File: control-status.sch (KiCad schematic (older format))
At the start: 11 parts

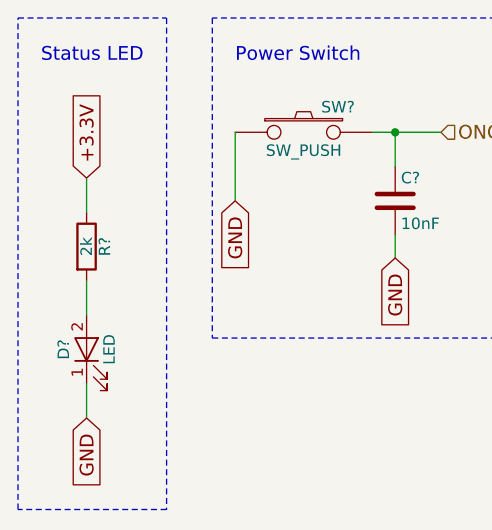
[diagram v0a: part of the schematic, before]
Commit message: this version contains the datasheets and the footprints of the parts
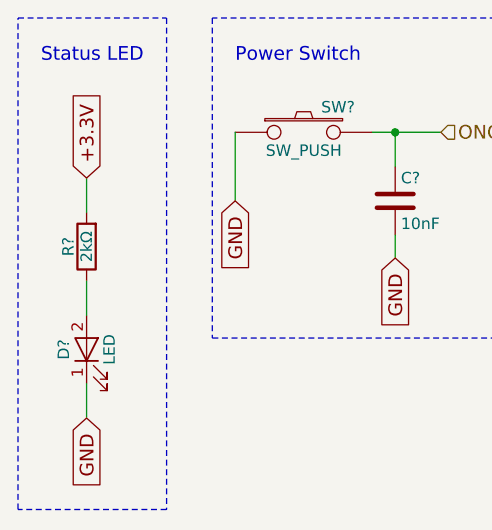
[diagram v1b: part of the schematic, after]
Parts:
- removed C? (x2): 100nF, symbol C
- removed R?: 2k, symbol R
- removed SW?: SW_PUSH, symbol SW_PUSH
- added C? (x2): 100nF, Capacitors_SMD:C_0603_HandSoldering, symbol C
- added R?: 2kΩ, Resistors_SMD:R_0603_HandSoldering, symbol R
- added SW?: SW_PUSH, water:EVQQ2202W, symbol SW_PUSH
- C?: footprint (none) -> Capacitors_SMD:C_0603_HandSoldering
- SW?: footprint (none) -> water:EVQQ2202W; alt (none) -> http://hu.farnell.com/alcoswitch-te-connectivity/fsm2jrt/ta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
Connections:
- net +3.3V: now also C?.1, R?.2
- net GND: now also C?.2, C?.2, SW?.2
- net RESET: now also C?.1, SW?.1
- net at D?.2 (A): now also R?.1
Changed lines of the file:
@@
 Comment4 ""
 $EndDescr
-$Comp
-L R R?
-U 1 1 59A3B272
-P 1050 1750
-F 0 "R?" V 1130 1750 50  0000 C CNN
-F 1 "2k" V 1050 1750 50  0000 C CNN
-F 2 "" V 980 1750 50  0001 C CNN
-F 3 "" H 1050 1750 50  0001 C CNN
-	1    1050 1750
-	1    0    0    -1
-$EndComp
 Text GLabel 1050 1450 1    60   Input ~ 0
 +3.3V
@@
 F 0 "SW?" H 2150 1360 50  0000 C CNN
 F 1 "SW_PUSH" H 2000 1170 50  0000 C CNN
-F 2 "" H 2000 1250 60  0000 C CNN
-F 3 "" H 2000 1250 60  0000 C CNN
+F 2 "water:EVQQ2202W" H 2000 1250 60  0001 C CNN
+F 3 "http://hu.farnell.com/panasonic-electronic-components/evqq2202w/switch-smd-6-5x6x2-5mm-3-5n/dp/1821261" H 2000 1250 60  0001 C CNN
+F 4 "http://hu.farnell.com/alcoswitch-te-connectivity/fsm2jrt/tactile-switch-spst-no-0-05a-24v/dp/2610957" H 2000 1250 60  0001 C CNN "alt"
 	1    2000 1250
 	1    0    0    -1
@@
 F 0 "C?" H 2425 1650 50  0000 L CNN
 F 1 "10nF" H 2425 1450 50  0000 L CNN
-F 2 "" H 2438 1400 50  0001 C CNN
-F 3 "" H 2400 1550 50  0001 C CNN
+F 2 "Capacitors_SMD:C_0603_HandSoldering" H 2438 1400 50  0001 C CNN
+F 3 "http://hu.farnell.com/multicomp/mc0603b103k500ct/cap-mlcc-x7r-10nf-50v-0603/dp/1759102" H 2400 1550 50  0001 C CNN
 	1    2400 1550
 	1    0    0    -1
@@
 Text Notes 4150 900  0    60   ~ 0
 Reset
-$Comp
-L SW_PUSH SW?
-U 1 1 59A3D04B
-P 5200 1350
-F 0 "SW?" H 5350 1460 50  0000 C CNN
-F 1 "SW_PUSH" H 5200 1270 50  0000 C CNN
-F 2 "" H 5200 1350 60  0000 C CNN
-F 3 "" H 5200 1350 60  0000 C CNN
-	1    5200 1350
-	1    0    0    -1
-$EndComp
 Text GLabel 5650 1700 3    60   Input ~ 0
 GND
-$Comp
-L C C?
-U 1 1 59A3D4AC
-P 4900 1550
-F 0 "C?" H 4925 1650 50  0000 L CNN
-F 1 "100nF" H 4925 1450 50  0000 L CNN
-F 2 "" H 4938 1400 50  0001 C CNN
-F 3 "" H 4900 1550 50  0001 C CNN
-	1    4900 1550
-	1    0    0    -1
-$EndComp
 Text GLabel 4900 1700 3    60   Input ~ 0
 GND
 Text HLabel 4900 1300 1    60   Input ~ 0
 RESET
-$Comp
-L C C?
-U 1 1 59A3E1D3
-P 4150 1650
-F 0 "C?" H 4175 1750 50  0000 L CNN
-F 1 "100nF" H 4175 1550 50  0000 L CNN
-F 2 "" H 4188 1500 50  0001 C CNN
-F 3 "" H 4150 1650 50  0001 C CNN
-	1    4150 1650
-	1    0    0    -1
-$EndComp
 Text GLabel 4150 1950 3    60   Input ~ 0
 GND
@@
 Wire Notes Line
 	6400 3500 1200 3500
+$Comp
+L C C?
+U 1 1 59A6A0B2
+P 4900 1550
+F 0 "C?" H 4925 1650 50  0000 L CNN
+F 1 "100nF" H 4925 1450 50  0000 L CNN
+F 2 "Capacitors_SMD:C_0603_HandSoldering" H 4938 1400 30  0001 C CNN
+F 3 "hu.farnell.com/avx/06035c104kat2a/cap-mlcc-x7r-100nf-50v-0603/dp/1301804" H 4900 1550 60  0001 C CNN
+	1    4900 1550
+	1    0    0    -1
+$EndComp
+$Comp
+L C C?
+U 1 1 59A6A9F5
+P 4150 1650
+F 0 "C?" H 4175 1750 50  0000 L CNN
+F 1 "100nF" H 4175 1550 50  0000 L CNN
+F 2 "Capacitors_SMD:C_0603_HandSoldering" H 4188 1500 30  0001 C CNN
+F 3 "hu.farnell.com/avx/06035c104kat2a/cap-mlcc-x7r-100nf-50v-0603/dp/1301804" H 4150 1650 60  0001 C CNN
+	1    4150 1650
+	1    0    0    -1
+$EndComp
+$Comp
+L SW_PUSH SW?
+U 1 1 59A6C82D
+P 5200 1350
+F 0 "SW?" H 5350 1460 50  0000 C CNN
+F 1 "SW_PUSH" H 5200 1270 50  0000 C CNN
+F 2 "water:EVQQ2202W" H 5200 1350 60  0001 C CNN
+F 3 "http://hu.farnell.com/panasonic-electronic-components/evqq2202w/switch-smd-6-5x6x2-5mm-3-5n/dp/1821261" H 5200 1350 60  0001 C CNN
+F 4 "http://hu.farnell.com/alcoswitch-te-connectivity/fsm2jrt/tactile-switch-spst-no-0-05a-24v/dp/2610957" H 5200 1350 60  0001 C CNN "alt"
+	1    5200 1350
+	1    0    0    -1
+$EndComp
+$Comp
+L R R?
+U 1 1 59A95521
+P 1050 1750
+F 0 "R?" V 1130 1750 50  0000 C CNN
+F 1 "2kΩ" V 1050 1750 50  0000 C CNN
+F 2 "Resistors_SMD:R_0603_HandSoldering" V 980 1750 50  0001 C CNN
+F 3 "hu.farnell.com/multicomp/mcwr06x2001ftl/res-thick-film-2k-1-0-1w-0603/dp/2447319" H 1050 1750 50  0001 C CNN
+	1    1050 1750
+	-1   0    0    1
+$EndComp
 $EndSCHEMATC

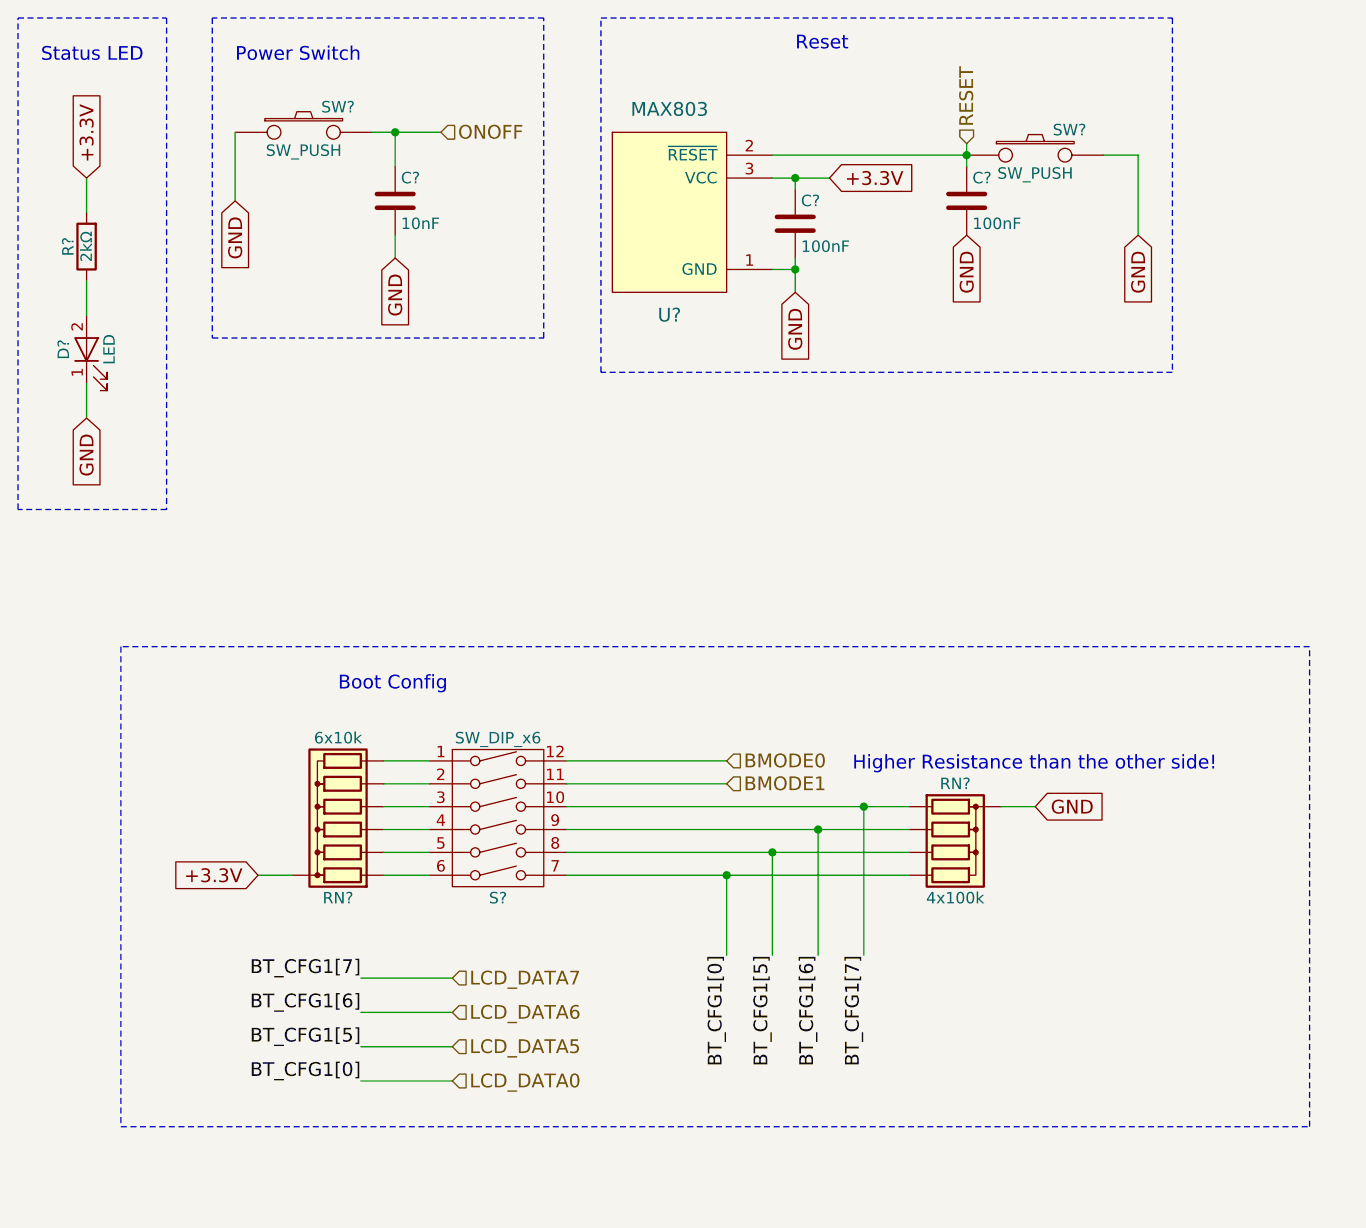
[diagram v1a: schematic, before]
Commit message: some issues fixed by the bugfixer; formal verification needed
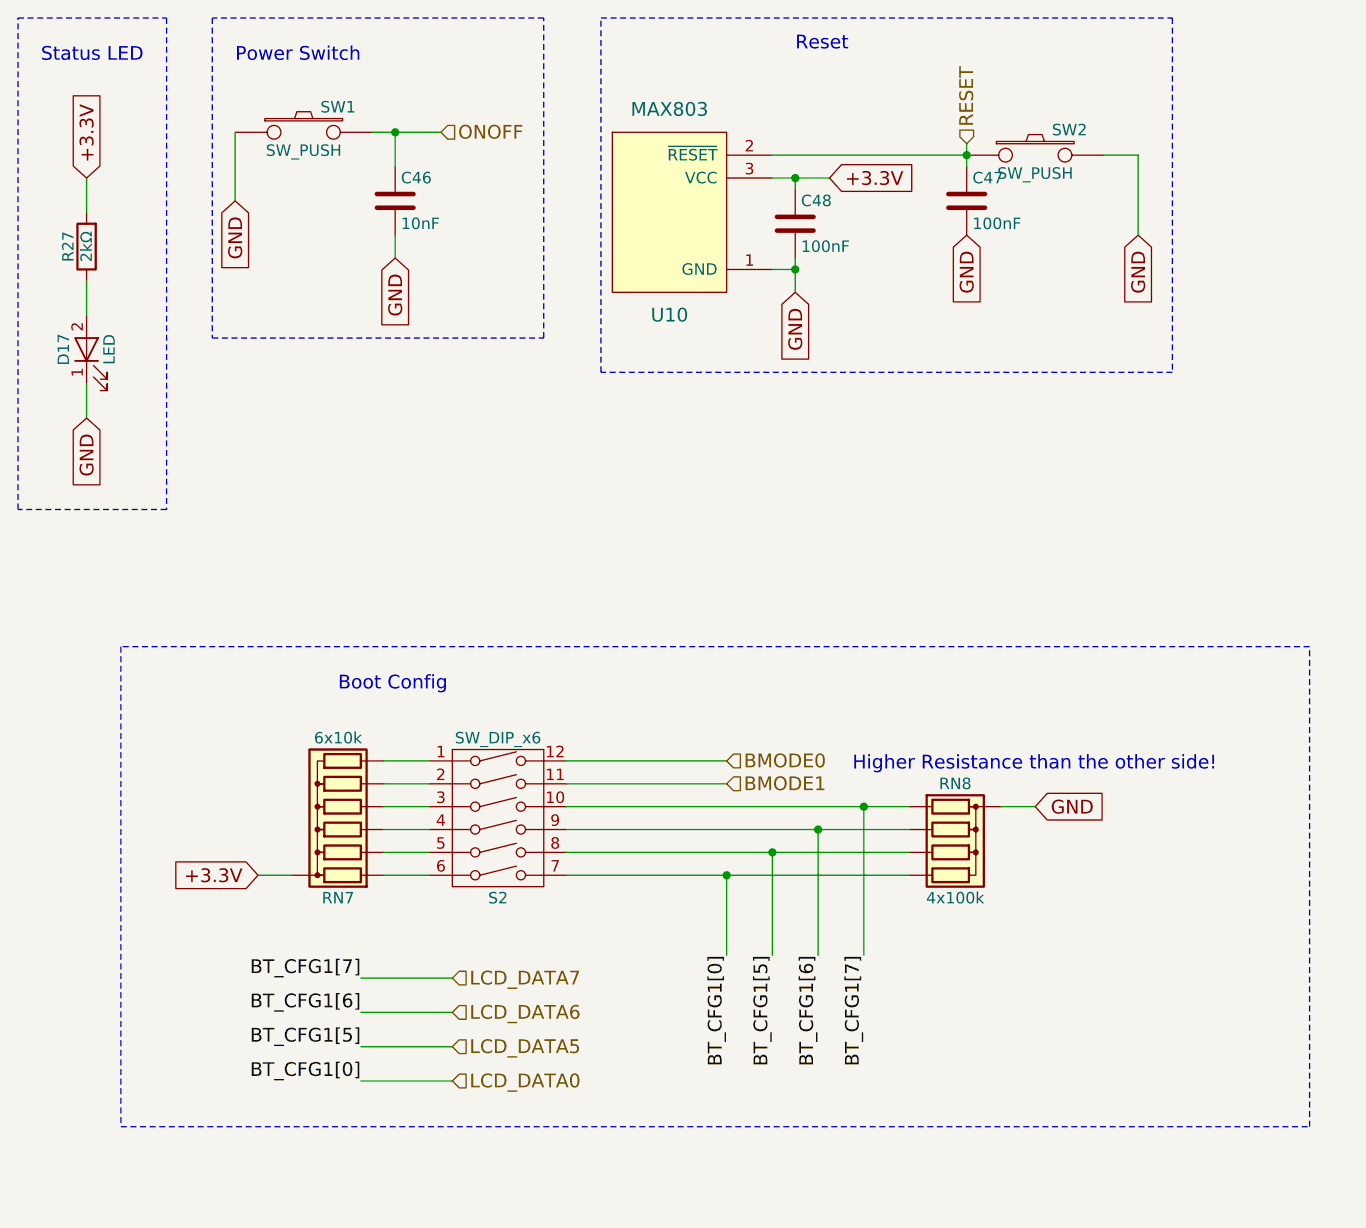
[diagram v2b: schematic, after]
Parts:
- gave numbers to parts that had none: 11
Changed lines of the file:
@@
 Status LED
 $Comp
-L LED D?
+L LED D17
 U 1 1 59A3B634
 P 1050 2200
-F 0 "D?" H 1050 2300 50  0000 C CNN
+F 0 "D17" H 1050 2300 50  0000 C CNN
 F 1 "LED" H 1050 2100 50  0000 C CNN
 F 2 "" H 1050 2200 50  0001 C CNN
@@
 Power Switch
 $Comp
-L SW_PUSH SW?
+L SW_PUSH SW1
 U 1 1 59A3BABB
 P 2000 1250
-F 0 "SW?" H 2150 1360 50  0000 C CNN
+F 0 "SW1" H 2150 1360 50  0000 C CNN
 F 1 "SW_PUSH" H 2000 1170 50  0000 C CNN
 F 2 "water:EVQQ2202W" H 2000 1250 60  0001 C CNN
@@
 GND
 $Comp
-L C C?
+L C C46
 U 1 1 59A3BB74
 P 2400 1550
-F 0 "C?" H 2425 1650 50  0000 L CNN
+F 0 "C46" H 2425 1650 50  0000 L CNN
 F 1 "10nF" H 2425 1450 50  0000 L CNN
 F 2 "Capacitors_SMD:C_0603_HandSoldering" H 2438 1400 50  0001 C CNN
@@
 GND
 $Comp
-L MAX803 U?
+L MAX803 U10
 U 1 1 59A3F36D
 P 3900 1200
-F 0 "U?" H 3600 350 60  0000 C CNN
+F 0 "U10" H 3600 350 60  0000 C CNN
 F 1 "MAX803" H 3600 1250 60  0000 C CNN
 F 2 "" H 3900 1200 60  0001 C CNN
@@
 +3.3V
 $Comp
-L SW_DIP_x6 S?
+L SW_DIP_x6 S2
 U 1 1 59A40F18
 P 2850 4250
-F 0 "S?" H 2850 3900 50  0000 C CNN
+F 0 "S2" H 2850 3900 50  0000 C CNN
 F 1 "SW_DIP_x6" H 2850 4600 50  0000 C CNN
 F 2 "" H 2800 4250 60  0000 C CNN
@@
 $EndComp
 $Comp
-L R_Network06 RN?
+L R_Network06 RN7
 U 1 1 59A4135A
 P 2150 4200
-F 0 "RN?" V 1750 4200 50  0000 C CNN
+F 0 "RN7" V 1750 4200 50  0000 C CNN
 F 1 "6x10k" V 2450 4200 50  0000 C CNN
 F 2 "Resistors_THT:R_Array_SIP7" V 2525 4200 50  0001 C CNN
@@
 BMODE1
 $Comp
-L R_Network04 RN?
+L R_Network04 RN8
 U 1 1 59A43007
 P 4850 4400
-F 0 "RN?" V 4550 4400 50  0000 C CNN
+F 0 "RN8" V 4550 4400 50  0000 C CNN
 F 1 "4x100k" V 5050 4400 50  0000 C CNN
 F 2 "Resistors_THT:R_Array_SIP5" V 5125 4400 50  0001 C CNN
@@
 	6400 3500 1200 3500
 $Comp
-L C C?
+L C C47
 U 1 1 59A6A0B2
 P 4900 1550
-F 0 "C?" H 4925 1650 50  0000 L CNN
+F 0 "C47" H 4925 1650 50  0000 L CNN
 F 1 "100nF" H 4925 1450 50  0000 L CNN
 F 2 "Capacitors_SMD:C_0603_HandSoldering" H 4938 1400 30  0001 C CNN
@@
 $EndComp
 $Comp
-L C C?
+L C C48
 U 1 1 59A6A9F5
 P 4150 1650
-F 0 "C?" H 4175 1750 50  0000 L CNN
+F 0 "C48" H 4175 1750 50  0000 L CNN
 F 1 "100nF" H 4175 1550 50  0000 L CNN
 F 2 "Capacitors_SMD:C_0603_HandSoldering" H 4188 1500 30  0001 C CNN
@@
 $EndComp
 $Comp
-L SW_PUSH SW?
+L SW_PUSH SW2
 U 1 1 59A6C82D
 P 5200 1350
-F 0 "SW?" H 5350 1460 50  0000 C CNN
+F 0 "SW2" H 5350 1460 50  0000 C CNN
 F 1 "SW_PUSH" H 5200 1270 50  0000 C CNN
 F 2 "water:EVQQ2202W" H 5200 1350 60  0001 C CNN
@@
 $EndComp
 $Comp
-L R R?
+L R R27
 U 1 1 59A95521
 P 1050 1750
-F 0 "R?" V 1130 1750 50  0000 C CNN
+F 0 "R27" V 1130 1750 50  0000 C CNN
 F 1 "2kΩ" V 1050 1750 50  0000 C CNN
 F 2 "Resistors_SMD:R_0603_HandSoldering" V 980 1750 50  0001 C CNN
